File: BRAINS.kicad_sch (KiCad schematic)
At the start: 9 parts, among them IC1 Z80CPU-DIP-SOCKET, IC2 Aries 40-600-21

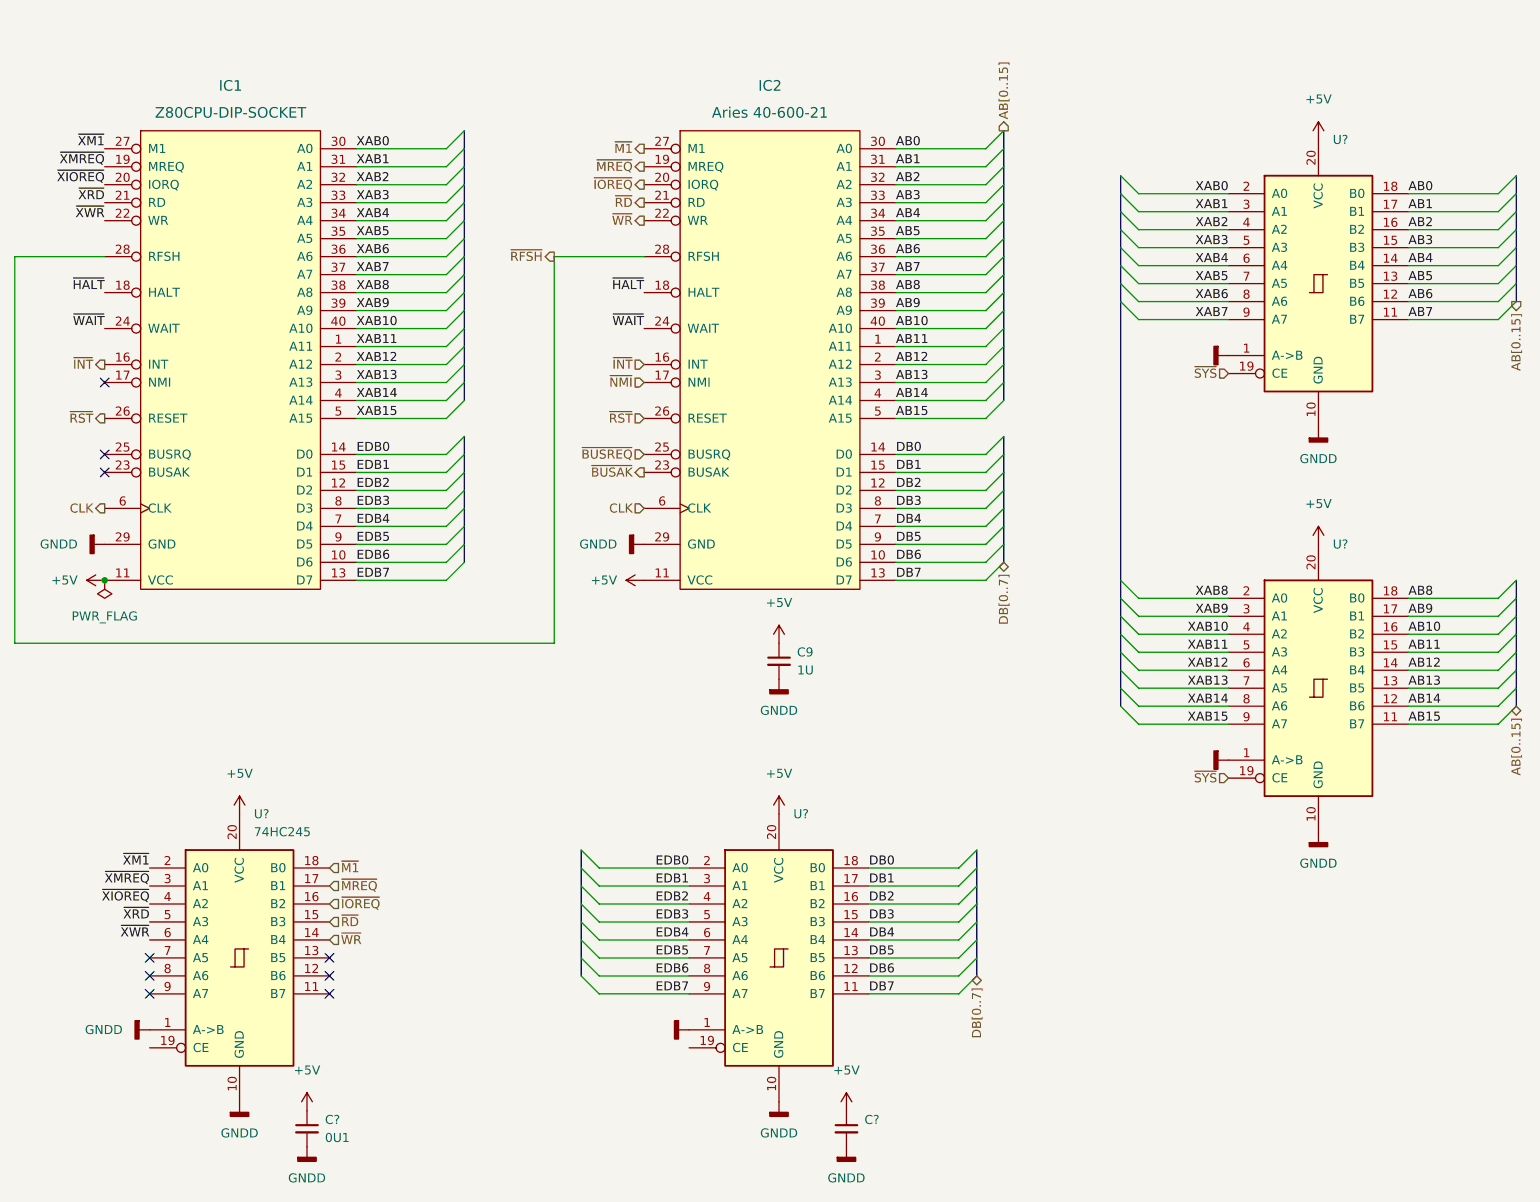
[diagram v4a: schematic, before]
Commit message: updated 84c10 pinout, apparently never checked for validity.... further simplification of dma and timer system (removed mode 2 interrupt structure, and interrupts in general) cleaned up vhdl code for 1508, still need testing to ensure functionality and that it even fits in the 1508....
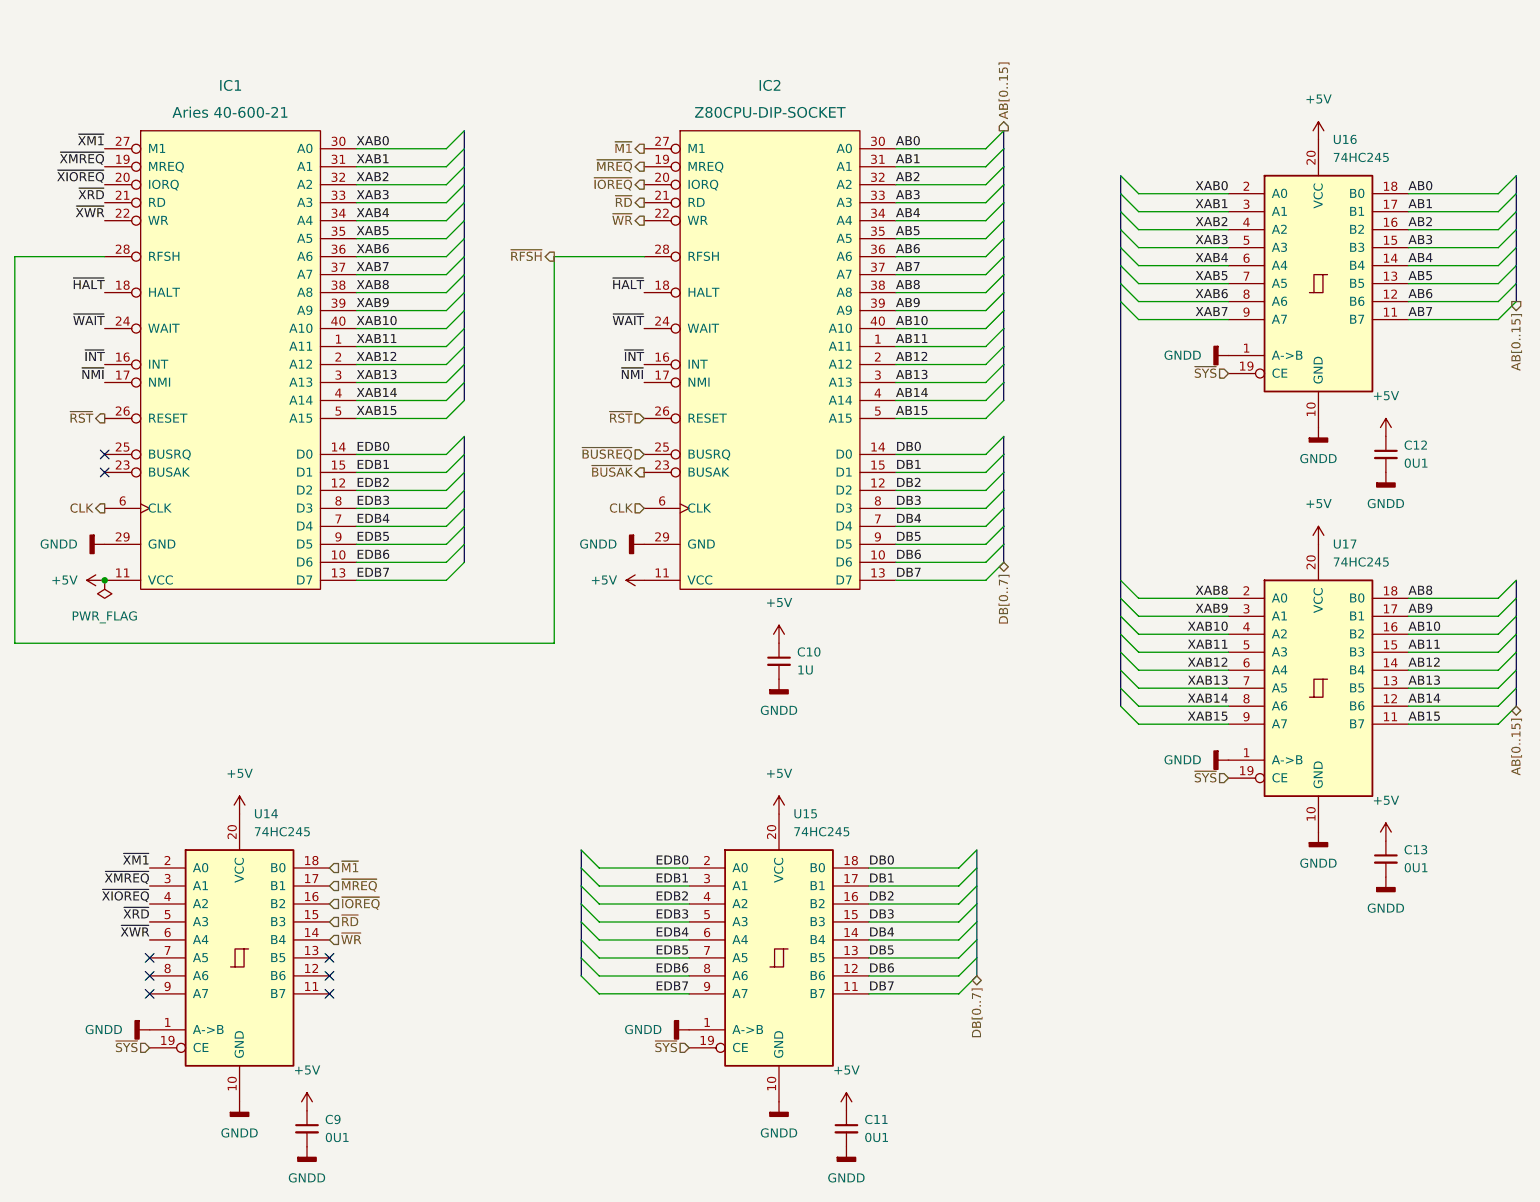
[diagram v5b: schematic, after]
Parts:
- added C12, C13: 0U1, Capacitor_SMD:C_1206_3216Metric, symbol Device:C_Small
- C11: renamed from C?; value (none) -> 0U1; footprint (none) -> Capacitor_SMD:C_1206_3216Metric
- IC1: renamed from IC2; footprint Package_DIP:DIP-40_W15.24mm_Socket -> (none)
- IC2: renamed from IC1; footprint Package_DIP:DIP-40_W15.24mm_Socket -> (none)
- U14: renamed from U?; footprint (none) -> Package_SO:TSSOP-20_4.4x6.5mm_P0.65mm
- U15, U16, U17: renamed from U?; value (none) -> 74HC245; footprint (none) -> Package_SO:TSSOP-20_4.4x6.5mm_P0.65mm
- gave numbers to parts that had none: 1
- renumbered C9 to C10
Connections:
- net +5V: now also C12.1, C13.1
- net AB0: now also IC2.30 (A0); no longer IC1.30 (A0)
- net AB1: now also IC2.31 (A1); no longer IC1.31 (A1)
- net AB10: now also IC2.40 (A10); no longer IC1.40 (A10)
- net AB11: now also IC2.1 (A11); no longer IC1.1 (A11)
- net AB12: now also IC2.2 (A12); no longer IC1.2 (A12)
- net AB13: now also IC2.3 (A13); no longer IC1.3 (A13)
- net AB14: now also IC2.4 (A14); no longer IC1.4 (A14)
- net AB15: now also IC2.5 (A15); no longer IC1.5 (A15)
- net AB2: now also IC2.32 (A2); no longer IC1.32 (A2)
- net AB3: now also IC2.33 (A3); no longer IC1.33 (A3)
- net AB4: now also IC2.34 (A4); no longer IC1.34 (A4)
- net AB5: now also IC2.35 (A5); no longer IC1.35 (A5)
- net AB6: now also IC2.36 (A6); no longer IC1.36 (A6)
- net AB7: now also IC2.37 (A7); no longer IC1.37 (A7)
- net AB8: now also IC2.38 (A8); no longer IC1.38 (A8)
- net AB9: now also IC2.39 (A9); no longer IC1.39 (A9)
- net DB0: now also IC2.14 (D0); no longer IC1.14 (D0)
- net DB1: now also IC2.15 (D1); no longer IC1.15 (D1)
- net DB2: now also IC2.12 (D2); no longer IC1.12 (D2)
- net DB3: now also IC2.8 (D3); no longer IC1.8 (D3)
- net DB4: now also IC2.7 (D4); no longer IC1.7 (D4)
- net DB5: now also IC2.9 (D5); no longer IC1.9 (D5)
- net DB6: now also IC2.10 (D6); no longer IC1.10 (D6)
- net DB7: now also IC2.13 (D7); no longer IC1.13 (D7)
- net EDB0: now also IC1.14 (D0); no longer IC2.14 (D0)
- net EDB1: now also IC1.15 (D1); no longer IC2.15 (D1)
- net EDB2: now also IC1.12 (D2); no longer IC2.12 (D2)
- net EDB3: now also IC1.8 (D3); no longer IC2.8 (D3)
- net EDB4: now also IC1.7 (D4); no longer IC2.7 (D4)
- net EDB5: now also IC1.9 (D5); no longer IC2.9 (D5)
- net EDB6: now also IC1.10 (D6); no longer IC2.10 (D6)
- net EDB7: now also IC1.13 (D7); no longer IC2.13 (D7)
- net GNDD: now also C12.2, C13.2
- net XAB0: now also IC1.30 (A0); no longer IC2.30 (A0)
- net XAB1: now also IC1.31 (A1); no longer IC2.31 (A1)
- net XAB10: now also IC1.40 (A10); no longer IC2.40 (A10)
- net XAB11: now also IC1.1 (A11); no longer IC2.1 (A11)
- net XAB12: now also IC1.2 (A12); no longer IC2.2 (A12)
- net XAB13: now also IC1.3 (A13); no longer IC2.3 (A13)
- net XAB14: now also IC1.4 (A14); no longer IC2.4 (A14)
- net XAB15: now also IC1.5 (A15); no longer IC2.5 (A15)
- net XAB2: now also IC1.32 (A2); no longer IC2.32 (A2)
- net XAB3: now also IC1.33 (A3); no longer IC2.33 (A3)
- net XAB4: now also IC1.34 (A4); no longer IC2.34 (A4)
- net XAB5: now also IC1.35 (A5); no longer IC2.35 (A5)
- net XAB6: now also IC1.36 (A6); no longer IC2.36 (A6)
- net XAB7: now also IC1.37 (A7); no longer IC2.37 (A7)
- net XAB8: now also IC1.38 (A8); no longer IC2.38 (A8)
- net XAB9: now also IC1.39 (A9); no longer IC2.39 (A9)
- net ~{BUSAK}: now also IC2.23 (BUSAK); no longer IC1.23 (BUSAK)
- net ~{BUSREQ}: now also IC2.25 (BUSRQ); no longer IC1.25 (BUSRQ)
- net ~{IOREQ}: now also IC2.20 (IORQ); no longer IC1.20 (IORQ)
- net ~{M1}: now also IC2.27 (M1); no longer IC1.27 (M1)
- net ~{MREQ}: now also IC2.19 (MREQ); no longer IC1.19 (MREQ)
- net ~{NMI}: now also IC2.17 (NMI)
- net ~{RD}: now also IC2.21 (RD); no longer IC1.21 (RD)
- net ~{SYS}: now also U14.19 (CE), U15.19 (CE)
- net ~{WR}: now also IC2.22 (WR); no longer IC1.22 (WR)
- net ~{XIOREQ}: now also IC1.20 (IORQ); no longer IC2.20 (IORQ)
- net ~{XM1}: now also IC1.27 (M1); no longer IC2.27 (M1)
- net ~{XMREQ}: now also IC1.19 (MREQ); no longer IC2.19 (MREQ)
- net ~{XRD}: now also IC1.21 (RD); no longer IC2.21 (RD)
- net ~{XWR}: now also IC1.22 (WR); no longer IC2.22 (WR)
- no-connect marks 9 -> 8
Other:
- moved on the sheet: IC1, IC2

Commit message: forgot to actually add the previous fixes to kicad
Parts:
- IC1, IC2: footprint (none) -> Package_DIP:DIP-40_W15.24mm_Socket
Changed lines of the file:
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@@
       (effects (font (size 1.4986 1.4986)))
     )
-    (property "Footprint" "" (id 2) (at 130.81 66.04 0)
+    (property "Footprint" "Package_DIP:DIP-40_W15.24mm_Socket" (id 2) (at 130.81 66.04 0)
       (effects (font (size 1.27 1.27)) hide)
     )
@@
       (effects (font (size 1.4986 1.4986)))
     )
-    (property "Footprint" "" (id 2) (at 54.61 66.04 0)
+    (property "Footprint" "Package_DIP:DIP-40_W15.24mm_Socket" (id 2) (at 54.61 66.04 0)
       (effects (font (size 1.27 1.27)) hide)
     )

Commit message: fixed logic errors (me being dumb forgetting associativity of ops, and fixed write only system databus on interposer
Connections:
- net GNDD: no longer U15.1 (A->B)
- new net DIR: U15.1 (A->B)
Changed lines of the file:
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@@
+    (effects (font (size 1.27 1.27)) (justify right))
+  )
+  (hierarchical_label "DIR" (shape input) (at 120.65 149.86 180)
     (effects (font (size 1.27 1.27)) (justify right))
   )
@@
     (pin "9")
   )
-  (symbol (lib_id "power:GNDD") (at 120.65 149.86 270) (unit 1)
-    (in_bom yes) (on_board yes) (fields_autoplaced)
-    (property "Reference" "#PWR067" (id 0) (at 114.3 149.86 0)
-      (effects (font (size 1.27 1.27)) hide)
-    )
-    (property "Value" "GNDD" (id 1) (at 116.84 149.8599 90)
-      (effects (font (size 1.27 1.27)) (justify right))
-    )
-    (property "Footprint" "" (id 2) (at 120.65 149.86 0)
-      (effects (font (size 1.27 1.27)) hide)
-    )
-    (property "Datasheet" "" (id 3) (at 120.65 149.86 0)
-      (effects (font (size 1.27 1.27)) hide)
-    )
-    (pin "1")
-  )
   (symbol (lib_id "Device:C_Small") (at 133.35 97.79 0) (unit 1)

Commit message: Added R5: a pull-up resistor for the /BUSREQ pin
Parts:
- added R5: 10k, Resistor_SMD:R_0603_1608Metric, symbol Device:R
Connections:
- net +5V: now also R5.1
- net ~{BUSREQ}: now also R5.2
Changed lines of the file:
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@@
+    (stroke (width 0) (type default) (color 0 0 0 0))
+  )
+  (wire (pts (xy 90.17 114.554) (xy 93.218 114.554))
     (stroke (width 0) (type default) (color 0 0 0 0))
   )
@@
   )
   (wire (pts (xy 120.65 129.54) (xy 107.95 129.54))
+    (stroke (width 0) (type default) (color 0 0 0 0))
+  )
+  (wire (pts (xy 93.218 114.554) (xy 93.218 112.776))
     (stroke (width 0) (type default) (color 0 0 0 0))
   )
@@
     (effects (font (size 1.27 1.27)) (justify right))
   )
+  (hierarchical_label "~{BUSREQ}" (shape input) (at 90.17 114.554 180)
+    (effects (font (size 1.27 1.27)) (justify right))
+  )
   (hierarchical_label "DB[0..7]" (shape bidirectional) (at 165.1 83.82 270)
     (effects (font (size 1.27 1.27)) (justify right))
@@
     )
     (pin "1")
+  )
+  (symbol (lib_id "Device:R") (at 93.218 108.966 0) (unit 1)
+    (in_bom yes) (on_board yes) (fields_autoplaced)
+    (property "Reference" "R5" (id 0) (at 95.25 107.6959 0)
+      (effects (font (size 1.27 1.27)) (justify left))
+    )
+    (property "Value" "10k" (id 1) (at 95.25 110.2359 0)
+      (effects (font (size 1.27 1.27)) (justify left))
+    )
+    (property "Footprint" "Resistor_SMD:R_0603_1608Metric" (id 2) (at 91.44 108.966 90)
+      (effects (font (size 1.27 1.27)) hide)
+    )
+    (property "Datasheet" "~" (id 3) (at 93.218 108.966 0)
+      (effects (font (size 1.27 1.27)) hide)
+    )
+    (pin "1")
+    (pin "2")
   )
   (symbol (lib_id "power:GNDD") (at 133.35 100.33 0) (unit 1)
@@
     (pin "2")
   )
+  (symbol (lib_id "power:+5V") (at 93.218 105.156 0) (unit 1)
+    (in_bom yes) (on_board yes) (fields_autoplaced)
+    (property "Reference" "#PWR031" (id 0) (at 93.218 108.966 0)
+      (effects (font (size 1.27 1.27)) hide)
+    )
+    (property "Value" "+5V" (id 1) (at 93.218 99.441 0))
+    (property "Footprint" "" (id 2) (at 93.218 105.156 0)
+      (effects (font (size 1.27 1.27)) hide)
+    )
+    (property "Datasheet" "" (id 3) (at 93.218 105.156 0)
+      (effects (font (size 1.27 1.27)) hide)
+    )
+    (pin "1")
+  )
   (symbol (lib_id "74xx:74HC245") (at 57.15 139.7 0) (unit 1)
